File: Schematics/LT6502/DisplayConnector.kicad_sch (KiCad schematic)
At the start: 11 parts, among them J5 Conn_02x20_Odd_Even, U8 TXS0108, U9 TXS0108

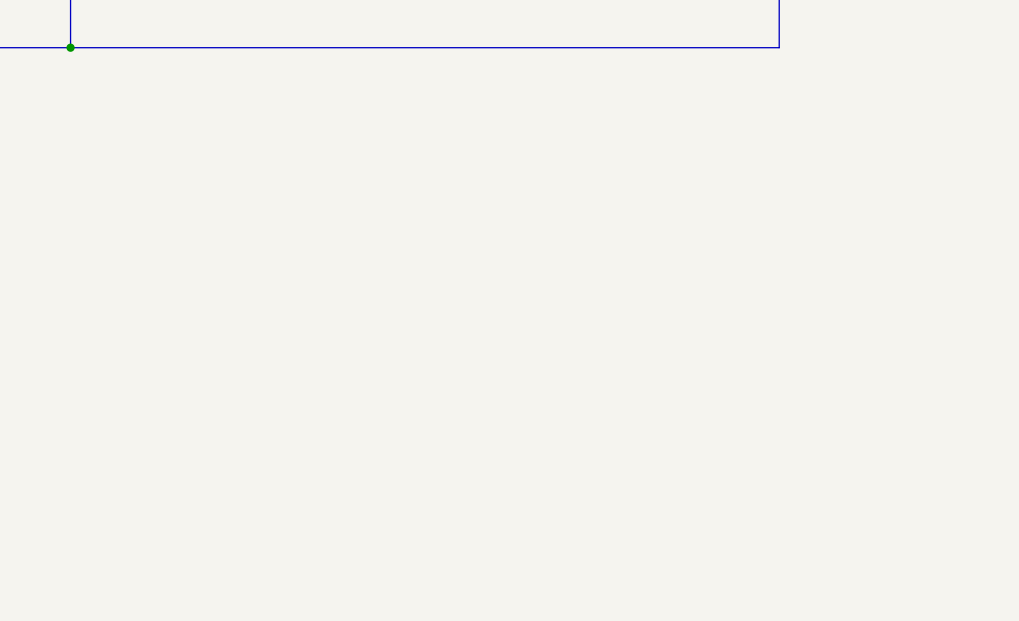
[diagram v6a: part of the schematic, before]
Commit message: Updated Schematics
Added bulk capacitance with higher ESR to help with display PLL starting
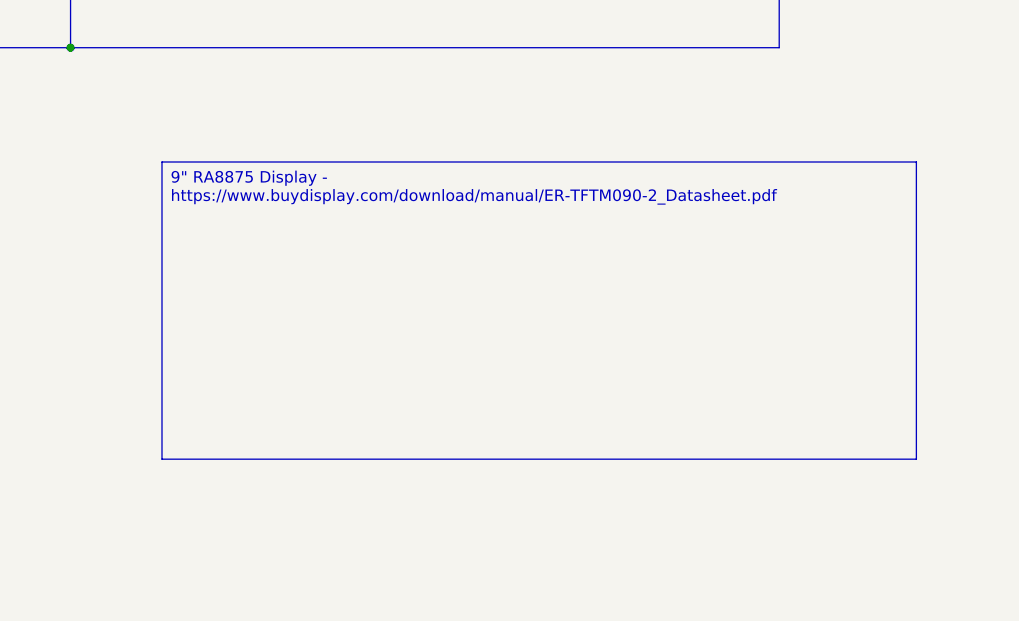
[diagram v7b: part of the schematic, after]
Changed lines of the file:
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@@
 	(generator_version "9.0")
 	(paper "A4")
+	(text_box "9\" RA8875 Display - https://www.buydisplay.com/download/manual/ER-TFTM090-2_Datasheet.pdf"
+		(exclude_from_sim no)
+		(at 165.1 129.54 0)
+		(size 83.82 33.02)
+		(margins 0.9525 0.9525 0.9525 0.9525)
+		(stroke
+			(width 0)
+			(type solid)
+		)
+		(fill
+			(type none)
+		)
+		(effects
+			(font
+				(size 1.27 1.27)
+			)
+			(justify left top)
+		)
+	)
 	(junction
 		(at 184.15 86.36)
